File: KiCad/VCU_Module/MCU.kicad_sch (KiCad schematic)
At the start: 27 parts, among them IC1 STM32C092RCT6, J11 Conn_ST_STDC14, Q3 2N7002, SW2 SW_Push, U6 MCP2562FDT-H_SN

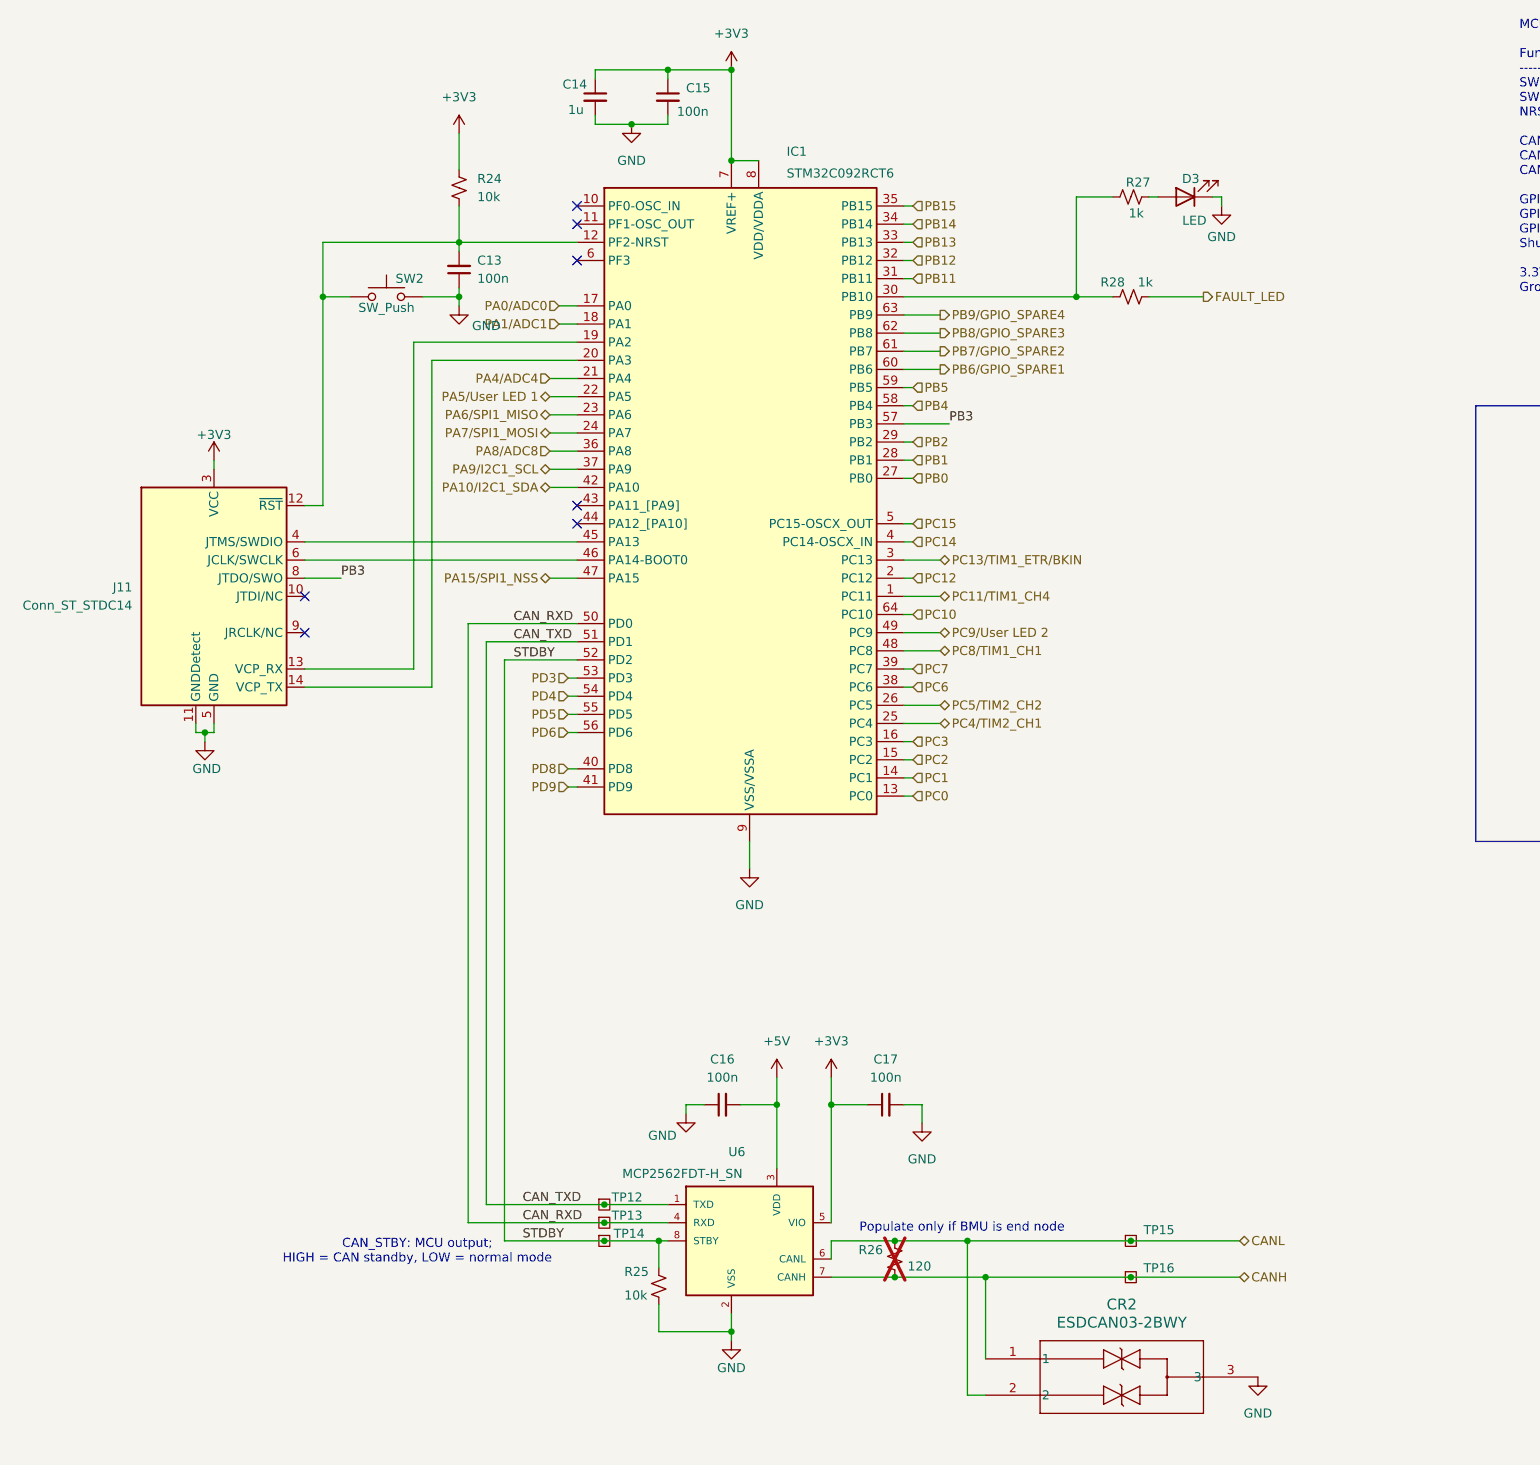
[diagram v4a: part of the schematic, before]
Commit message: fixed all socket header connections, placed and routed every component on PCB, added all 3d models to footprints
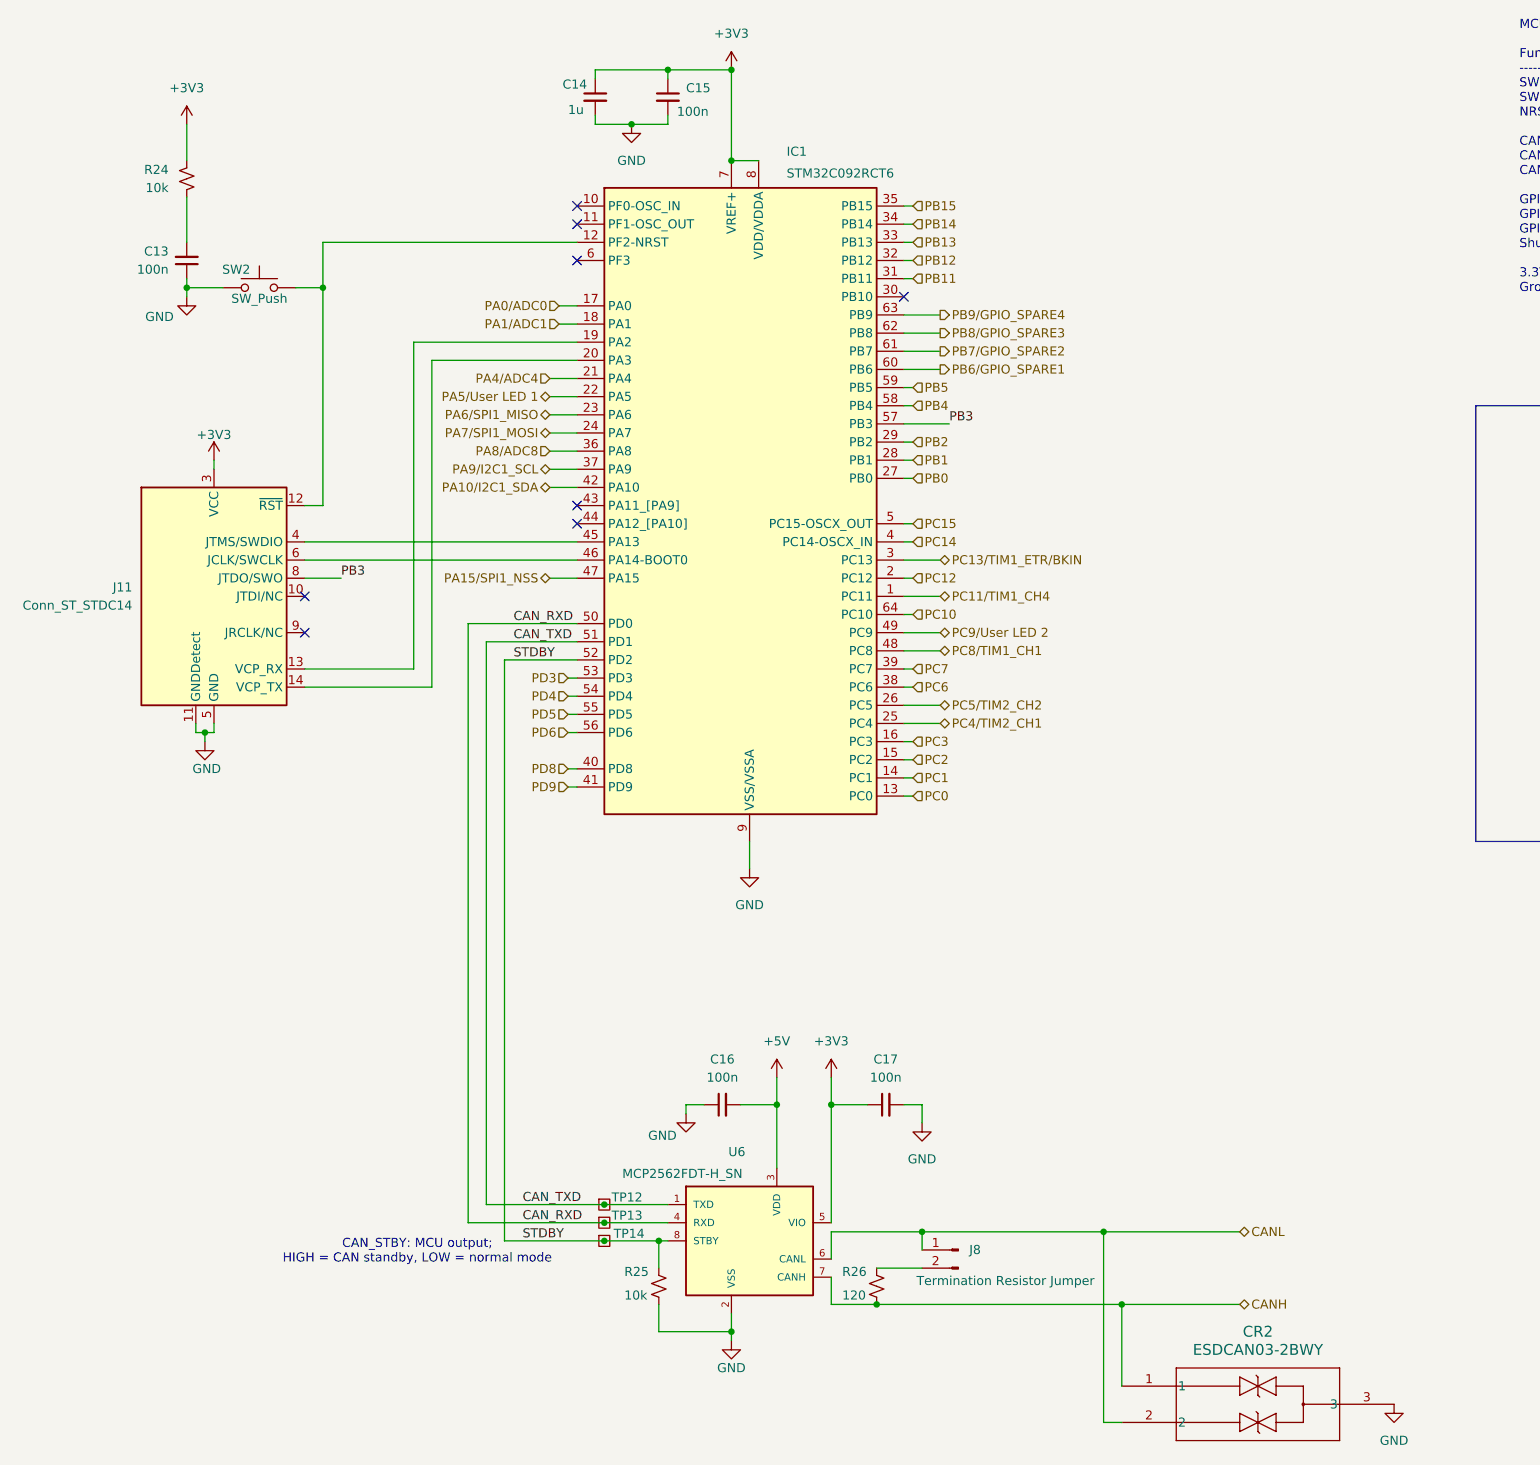
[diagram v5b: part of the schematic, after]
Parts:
- removed D3: LED, LED_SMD:LED_0805_2012Metric_Pad1.15x1.40mm_HandSolder, symbol Device:LED
- removed R27, R28: 1k, Resistor_SMD:R_0805_2012Metric, symbol Device:R_Small_US
- removed TP15, TP16: TestPoint_Small, TestPoint:TestPoint_THTPad_D1.5mm_Drill0.7mm, symbol Connector:TestPoint_Square
- added J8: Termination Resistor Jumper, Connector_PinHeader_2.54mm:PinHeader_1x02_P2.54mm_Vertical, symbol Connector:Conn_01x02_Pin
- R26: DPN 311-120CRCT-ND -> 311-10.0KCRCT-ND; MPN RC0805FR-07120RL -> RC0805FR-0710KL; Purchase Link https://www.digikey.com/en/products/detail/yageo/RC0805FR-07120RL/727575 -> https://www.digikey.com/en/products/detail/yageo/RC0805FR-0710KL/727535; now fitted
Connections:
- net CANL: now also J8.1 (Pin_1); no longer R26.1
- net at IC1.12 (PF2-NRST), J11.12 (~{RST}), SW2.1: no longer C13.2, R24.2
- new net: J8.2 (Pin_2), R26.1
- new net: C13.2, R24.2
- no-connect marks 7 -> 8
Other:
- note removed: "Populate only if BMU is end node"
- moved on the sheet: CR2

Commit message: updated pcb from sohams adjustments to schematic
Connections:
- net +3V3 renamed 3V3
- net +5V renamed 5V
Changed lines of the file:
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@@
 			)
 		)
-		(property "Value" "+3V3"
-			(at 182.88 44.45 0)
-			(show_name no)
-			(do_not_autoplace no)
-			(effects
-				(font
-					(size 1.27 1.27)
-				)
+		(property "Value" "3V3"
+			(at 185.42 48.2599 0)
+			(show_name no)
+			(do_not_autoplace no)
+			(effects
+				(font
+					(size 1.27 1.27)
+				)
+				(justify left)
 			)
 		)
@@
 		(in_pos_files yes)
 		(dnp no)
-		(fields_autoplaced yes)
 		(property "Reference" "#PWR044"
 			(at 189.23 194.31 0)
@@
 			)
 		)
-		(property "Value" "+5V"
-			(at 189.23 185.42 0)
-			(show_name no)
-			(do_not_autoplace no)
-			(effects
-				(font
-					(size 1.27 1.27)
-				)
+		(property "Value" "5V"
+			(at 187.706 186.69 0)
+			(show_name no)
+			(do_not_autoplace no)
+			(effects
+				(font
+					(size 1.27 1.27)
+				)
+				(justify left)
 			)
 		)
@@
 			)
 		)
-		(property "Value" "+3V3"
+		(property "Value" "3V3"
 			(at 110.49 100.584 0)
 			(show_name no)
@@
 			)
 		)
-		(property "Value" "+3V3"
-			(at 106.68 52.07 0)
-			(show_name no)
-			(do_not_autoplace no)
-			(effects
-				(font
-					(size 1.27 1.27)
-				)
+		(property "Value" "3V3"
+			(at 109.22 55.8799 0)
+			(show_name no)
+			(do_not_autoplace no)
+			(effects
+				(font
+					(size 1.27 1.27)
+				)
+				(justify right)
 			)
 		)
@@
 		(in_pos_files yes)
 		(dnp no)
-		(fields_autoplaced yes)
 		(property "Reference" "#PWR049"
 			(at 358.14 116.84 0)
@@
 			)
 		)
-		(property "Value" "+3V3"
-			(at 358.14 107.95 0)
-			(show_name no)
-			(do_not_autoplace no)
-			(effects
-				(font
-					(size 1.27 1.27)
-				)
+		(property "Value" "3V3"
+			(at 356.362 108.458 0)
+			(show_name no)
+			(do_not_autoplace no)
+			(effects
+				(font
+					(size 1.27 1.27)
+				)
+				(justify left)
 			)
 		)
@@
 		(in_pos_files yes)
 		(dnp no)
-		(fields_autoplaced yes)
 		(property "Reference" "#PWR045"
 			(at 196.85 194.31 0)
@@
 			)
 		)
-		(property "Value" "+3V3"
-			(at 196.85 185.42 0)
-			(show_name no)
-			(do_not_autoplace no)
-			(effects
-				(font
-					(size 1.27 1.27)
-				)
-			)
-		)
+		(property "Value" "3V3"
+			(at 195.326 185.928 0)
+			(show_name no)
+			(do_not_autoplace no)
+			(effects
+				(font
+					(size 1.27 1.27)
+				)
+				(justify left)
+			)
+		)

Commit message: schematic complete with new fuse holder and specs, just need to run ERC once more PCB component placement and traces done, still need to fix some DRC Errors and check warnings Still need to ensure all components are labeled properly with no overlapping silkscreen labels
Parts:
- removed Q3: 2N7002, Package_TO_SOT_SMD:SOT-23, symbol Transistor_FET:2N7002
- removed R10: 1M, Resistor_SMD:R_0805_2012Metric, symbol Device:R_Small_US
- removed R24: 10k, Resistor_SMD:R_0805_2012Metric, symbol Device:R_Small_US
- added CR3: ESDA051-1JY, VMS_Footprints:ESDA051-1JY, symbol ESDA051-1JY:ESDA051-1JY
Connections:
- net GND: now also CR3.2
- net PA5/User LED 1: now also D5.1 (K)
- net NRST: now reaches C13.2
- net NRST: now also IC1.12 (PF2-NRST), J11.12 (~{RST}), SW2.1, CR3.1
- net VCP_RX: now reaches J11.13 (VCP_RX)
- net VCP_RX: now also IC1.20 (PA3); no longer IC1.19 (PA2)
- net VCP_TX: now reaches J11.14 (VCP_TX)
- net VCP_TX: now also IC1.19 (PA2); no longer IC1.20 (PA3)
- net SWDIO: now reaches IC1.45 (PA13), J11.4 (JTMS/SWDIO)
- net SWCLK/BOOT0: now reaches IC1.46 (PA14-BOOT0), J11.6 (JCLK/SWCLK)
- net PB3 renamed SWO
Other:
- note added: "CAN FD"
- note added: "RST"
- note added: "STLINK"
- note removed: "User LEDs"
- moved on the sheet: C16, C17, CR2, J8, R25, R26, TP12, TP13, TP14, U6

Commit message: finished DRC checks and ERC checks in schematic and PCB, added many new components with purchase links to BOM, still need to double check previously added parts in BOM to ensure they are sufficient for higher voltage inputs
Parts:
- C13, C15, C16, C17: DIS DigiKey -> (none); DPN 311-1140-1-ND -> (none); MFR YAGEO -> (none); MPN CC0805KRX7R9BB104 -> (none); Purchase Link https://www.digikey.com/en/products/detail/yageo/CC0805KRX7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 -> (none)
- C14: DIS DigiKey -> (none); DPN 311-1365-1-ND -> (none); MFR YAGEO -> (none); MPN CC0805KKX7R7BB105 -> (none); Purchase Link https://www.digikey.com/en/products/detail/yageo/CC0805KKX7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 -> (none)
- CR3: DIS (none) -> DigiKey; DPN (none) -> 497-ESDA051-1JYCT-ND; MFR (none) -> STMicroelectronics; MPN (none) -> ESDA051-1JY; Purchase Link (none) -> https://www.digikey.com/en/products/detail/stmicroelectroni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
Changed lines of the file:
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@@
 			)
 		)
-		(property "Description" "Unpolarized capacitor, small symbol"
+		(property "Description" ""
 			(at 82.55 207.01 0)
 			(hide yes)
@@
 			)
 		)
-		(property "DIS" "DigiKey"
+		(property "DIS" ""
 			(at 82.55 207.01 90)
 			(hide yes)
@@
 			)
 		)
-		(property "DPN" "311-1140-1-ND"
+		(property "DPN" ""
 			(at 82.55 207.01 90)
 			(hide yes)
@@
 			)
 		)
-		(property "MFR" "YAGEO"
+		(property "MFR" ""
 			(at 82.55 207.01 90)
 			(hide yes)
@@
 			)
 		)
-		(property "MPN" "CC0805KRX7R9BB104"
+		(property "MPN" ""
 			(at 82.55 207.01 90)
 			(hide yes)
@@
 			)
 		)
-		(property "Purchase Link" "https://www.digikey.com/en/products/detail/yageo/CC0805KRX7R9BB104/302874"
+		(property "Purchase Link" ""
 			(at 82.55 207.01 90)
 			(hide yes)
@@
 			)
 		)
-		(property "Description" "Unpolarized capacitor, small symbol"
+		(property "Description" ""
 			(at 105.41 207.01 0)
 			(hide yes)
@@
 			)
 		)
-		(property "DIS" "DigiKey"
+		(property "DIS" ""
 			(at 105.41 207.01 90)
 			(hide yes)
@@
 			)
 		)
-		(property "DPN" "311-1140-1-ND"
+		(property "DPN" ""
 			(at 105.41 207.01 90)
 			(hide yes)
@@
 			)
 		)
-		(property "MFR" "YAGEO"
+		(property "MFR" ""
 			(at 105.41 207.01 90)
 			(hide yes)
@@
 			)
 		)
-		(property "MPN" "CC0805KRX7R9BB104"
+		(property "MPN" ""
 			(at 105.41 207.01 90)
 			(hide yes)
@@
 			)
 		)
-		(property "Purchase Link" "https://www.digikey.com/en/products/detail/yageo/CC0805KRX7R9BB104/302874"
+		(property "Purchase Link" ""
 			(at 105.41 207.01 90)
 			(hide yes)
@@
 			)
 		)
-		(property "Description" ""
+		(property "Description" "TVS Diode"
 			(at 44.45 67.31 0)
 			(hide yes)
@@
 			)
 		)
+		(property "DIS" "DigiKey"
+			(at 44.45 67.31 90)
+			(hide yes)
+			(show_name no)
+			(do_not_autoplace no)
+			(effects
+				(font
+					(size 1.27 1.27)
+				)
+			)
+		)
+		(property "DPN" "497-ESDA051-1JYCT-ND"
+			(at 44.45 67.31 90)
+			(hide yes)
+			(show_name no)
+			(do_not_autoplace no)
+			(effects
+				(font
+					(size 1.27 1.27)
+				)
+			)
+		)
+		(property "MFR" "STMicroelectronics"
+			(at 44.45 67.31 90)
+			(hide yes)
+			(show_name no)
+			(do_not_autoplace no)
+			(effects
+				(font
+					(size 1.27 1.27)
+				)
+			)
+		)
+		(property "MPN" "ESDA051-1JY"
+			(at 44.45 67.31 90)
+			(hide yes)
+			(show_name no)
+			(do_not_autoplace no)
+			(effects
+				(font
+					(size 1.27 1.27)
+				)
+			)
+		)
+		(property "Purchase Link" "https://www.digikey.com/en/products/detail/stmicroelectronics/ESDA051-1JY/11686344?s=N4IgTCBcDaIKIGUAiBBADAVgIwFosCkBNEAXQF8g"
+			(at 44.45 67.31 90)
+			(hide yes)
+			(show_name no)
+			(do_not_autoplace no)
+			(effects
+				(font
+					(size 1.27 1.27)
+				)
+			)
+		)
 		(pin "2"
 		)
@@
 			)
 		)
-		(property "Description" "Unpolarized capacitor, small symbol"
+		(property "Description" ""
 			(at 54.61 62.23 0)
 			(hide yes)
@@
 			)
 		)
-		(property "DIS" "DigiKey"
+		(property "DIS" ""
 			(at 54.61 62.23 0)
 			(hide yes)
@@
 			)
 		)
-		(property "DPN" "311-1140-1-ND"
+		(property "DPN" ""
 			(at 54.61 62.23 0)
 			(hide yes)
@@
 			)
 		)
-		(property "MFR" "YAGEO"
+		(property "MFR" ""
 			(at 54.61 62.23 0)
 			(hide yes)
@@
 			)
 		)
-		(property "MPN" "CC0805KRX7R9BB104"
+		(property "MPN" ""
 			(at 54.61 62.23 0)
 			(hide yes)
@@
 			)
 		)
-		(property "Purchase Link" "https://www.digikey.com/en/products/detail/yageo/CC0805KRX7R9BB104/302874"
+		(property "Purchase Link" ""
 			(at 54.61 62.23 0)
 			(hide yes)
@@
 			)
 		)
-		(property "Description" "Unpolarized capacitor, small symbol"
+		(property "Description" ""
 			(at 163.83 53.34 0)
 			(hide yes)
@@
 			)
 		)
-		(property "DIS" "DigiKey"
+		(property "DIS" ""
 			(at 163.83 53.34 0)
 			(hide yes)
@@
 			)
 		)
-		(property "DPN" "311-1365-1-ND"
+		(property "DPN" ""
 			(at 163.83 53.34 0)
 			(hide yes)
@@
 			)
 		)
-		(property "MFR" "YAGEO"
+		(property "MFR" ""
 			(at 163.83 53.34 0)
 			(hide yes)
@@
 			)
 		)
-		(property "MPN" "CC0805KKX7R7BB105"
+		(property "MPN" ""
 			(at 163.83 53.34 0)
 			(hide yes)
@@
 			)
 		)
-		(property "Purchase Link" "https://www.digikey.com/en/products/detail/yageo/CC0805KKX7R7BB105/2103103"
+		(property "Purchase Link" ""
 			(at 163.83 53.34 0)
 			(hide yes)
@@
 			)
 		)
-		(property "Description" "Unpolarized capacitor, small symbol"
+		(property "Description" ""
 			(at 173.99 53.34 0)
 			(hide yes)
@@
 			)
 		)
-		(property "DIS" "DigiKey"
+		(property "DIS" ""
 			(at 173.99 53.34 0)
 			(hide yes)
@@
 			)
 		)
-		(property "DPN" "311-1140-1-ND"
+		(property "DPN" ""
 			(at 173.99 53.34 0)
 			(hide yes)
@@
 			)
 		)
-		(property "MFR" "YAGEO"
+		(property "MFR" ""
 			(at 173.99 53.34 0)
 			(hide yes)
@@
 			)
 		)
-		(property "MPN" "CC0805KRX7R9BB104"
+		(property "MPN" ""
 			(at 173.99 53.34 0)
 			(hide yes)
@@
 			)
 		)
-		(property "Purchase Link" "https://www.digikey.com/en/products/detail/yageo/CC0805KRX7R9BB104/302874"
+		(property "Purchase Link" ""
 			(at 173.99 53.34 0)
 			(hide yes)
